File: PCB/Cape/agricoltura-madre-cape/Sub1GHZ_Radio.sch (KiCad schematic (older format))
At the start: 1 part

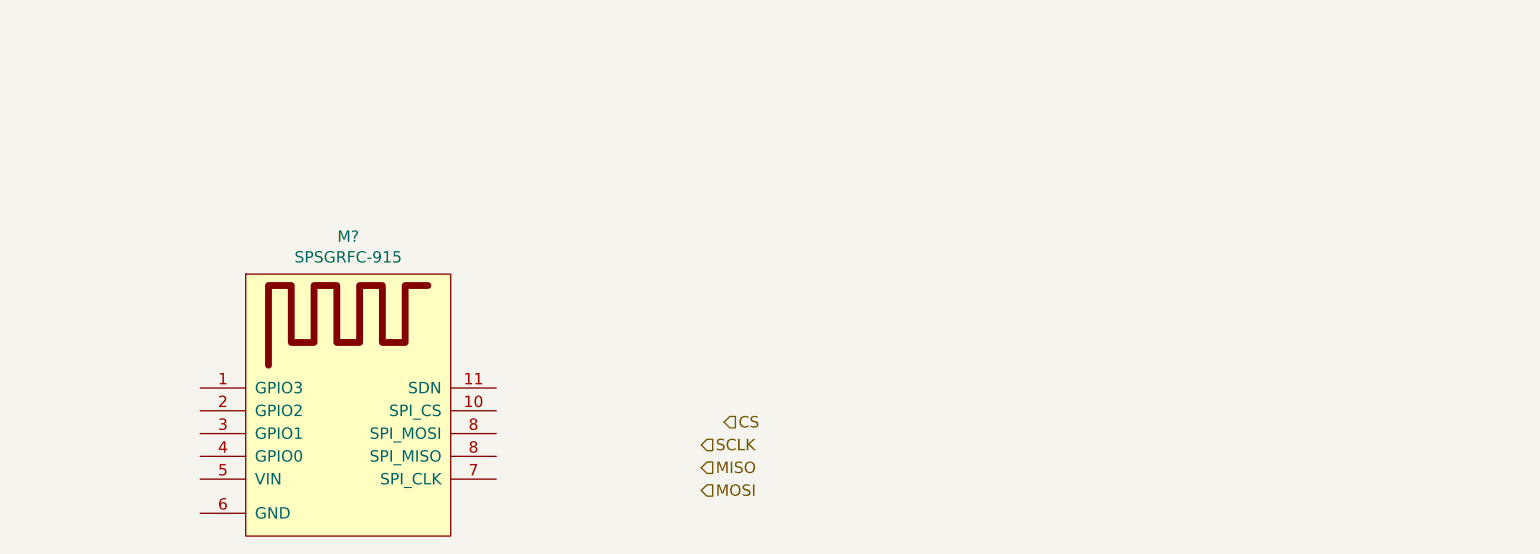
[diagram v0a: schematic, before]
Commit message: Datasheets and BBG version
Finished initial schematic for BBG Gateway version and added datasheets for ST sub 1GHZ RF hardware.
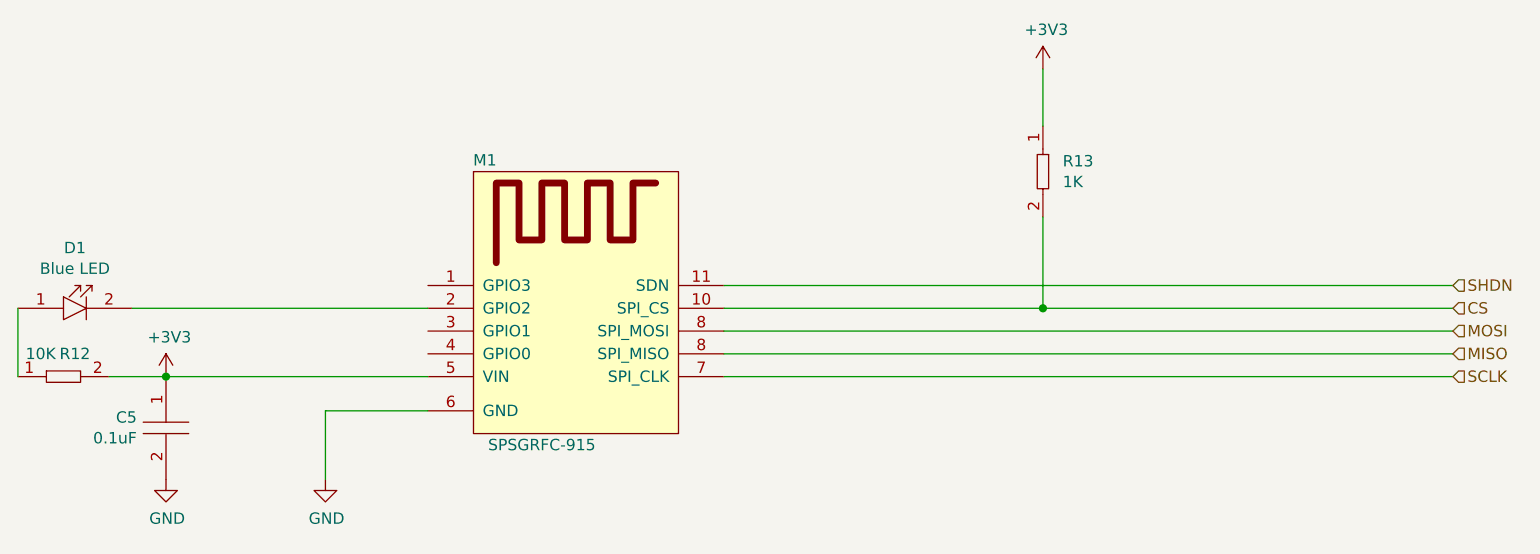
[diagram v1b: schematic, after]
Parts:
- added C5: C0402C104K9PACTU, AVR-KiCAD-Lib-Resistors:R0402, symbol AVR-KiCAD-Lib-Capacitors:C0402C104K9PACTU
- added D1: LTST-C194TBKT, AVR-KiCAD-Lib-Diodes:LED0603, symbol AVR-KiCAD-Lib-Diodes:LTST-C194TBKT
- added R12: RC0402FR-0710KL, AVR-KiCAD-Lib-Resistors:R0402, symbol AVR-KiCAD-Lib-Resistors:RC0402FR-0710KL
- added R13: RC0402FR-071KL, AVR-KiCAD-Lib-Resistors:R0402, symbol AVR-KiCAD-Lib-Resistors:RC0402FR-071KL
- gave numbers to parts that had none: 1
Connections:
- net CS: now also M1.10 (SPI_CS), R13.2
- net MISO: now also M1.8 (SPI_MOSI)
- net MOSI: now also M1.8 (SPI_MOSI)
- net SCLK: now also M1.7 (SPI_CLK)
- net SHDN: now reaches M1.11 (SDN)
- net at M1.2 (GPIO2): now also D1.2
- net +3V3: now reaches M1.5 (VIN)
- net +3V3: now also C5.1, R12.2, R13.1
- net GND: now reaches M1.6 (GND)
- net GND: now also C5.2
- new net: D1.1, R12.1
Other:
- moved on the sheet: M1
